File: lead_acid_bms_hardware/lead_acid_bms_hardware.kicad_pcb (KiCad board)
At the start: 2 copper layers, 88 x 52.3 mm, 72 parts, among them J1 debugging_connector, J2 battery_p, J3 battery_n, J4 bms_p, J5 bms_n, Q1 IRFZ44N, Q10 CJ2305, Q11 CJ2305, Q2 IRFZ44N, Q3 MMBT3904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

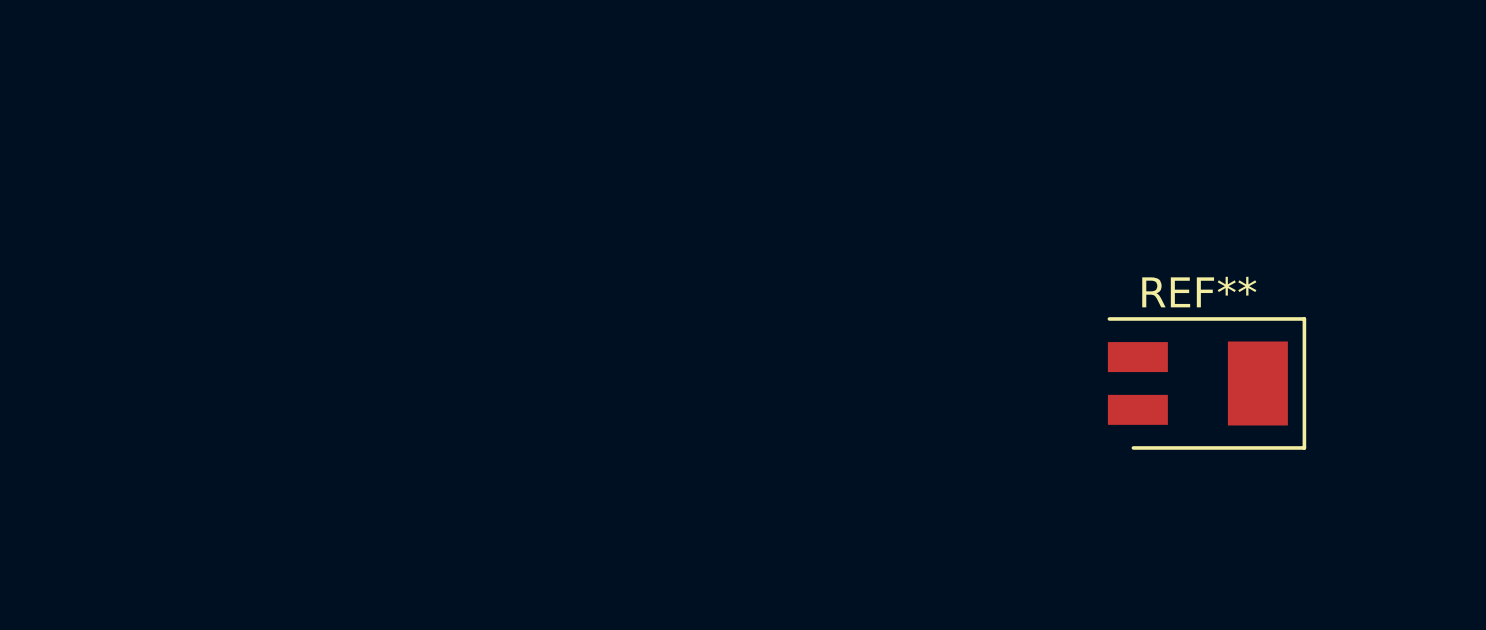
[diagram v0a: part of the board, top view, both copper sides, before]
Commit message: Added NTC for temperature measurements
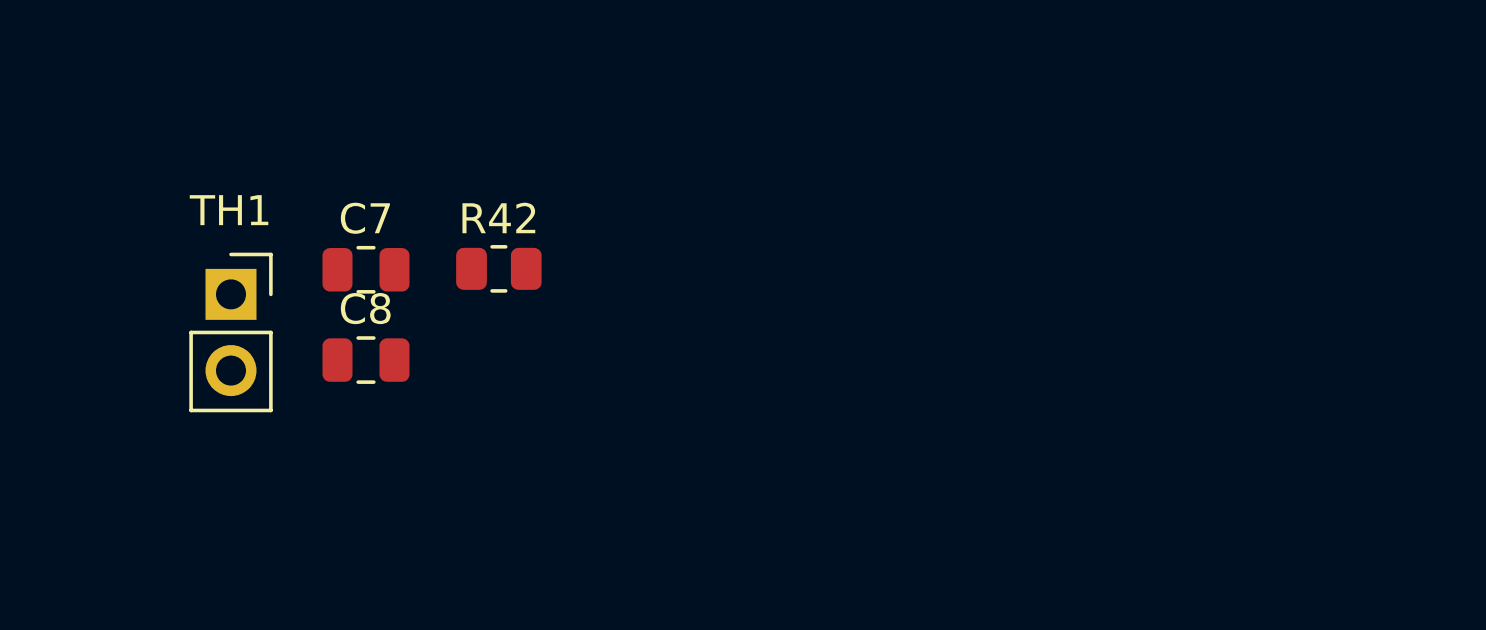
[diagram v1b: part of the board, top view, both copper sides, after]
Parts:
- removed REF**: D_SMB_Modified, Diode_SMD:D_SMB_Modified
- added C7: 100nF, Capacitor_SMD:C_0805_2012Metric, F.Cu at (153.3, 54.2)
- added C8: 100nF, Capacitor_SMD:C_0805_2012Metric, F.Cu at (153.3, 57.2)
- added R42: 10k, Resistor_SMD:R_0805_2012Metric, F.Cu at (157.7, 54.2)
- added TH1: 3977K, Connector_PinSocket_2.54mm:PinSocket_1x02_P2.54mm_Vertical, F.Cu at (148.8, 55.0)
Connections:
- U3 pad 19: unconnected-(U3-Pad19) -> THERMISTOR_ADC_VOUT
